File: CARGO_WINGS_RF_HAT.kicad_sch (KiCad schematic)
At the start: 7 parts, among them J1 RPi_GPIO, J2 ESP Prog, J3 Conn_01x04_Socket, J4 Conn_01x04_Socket, J8 S2B-PH-K-S(LF)(SN), U1 DWM1000, U2 ESP32-S3-WROOM-1-N8R2

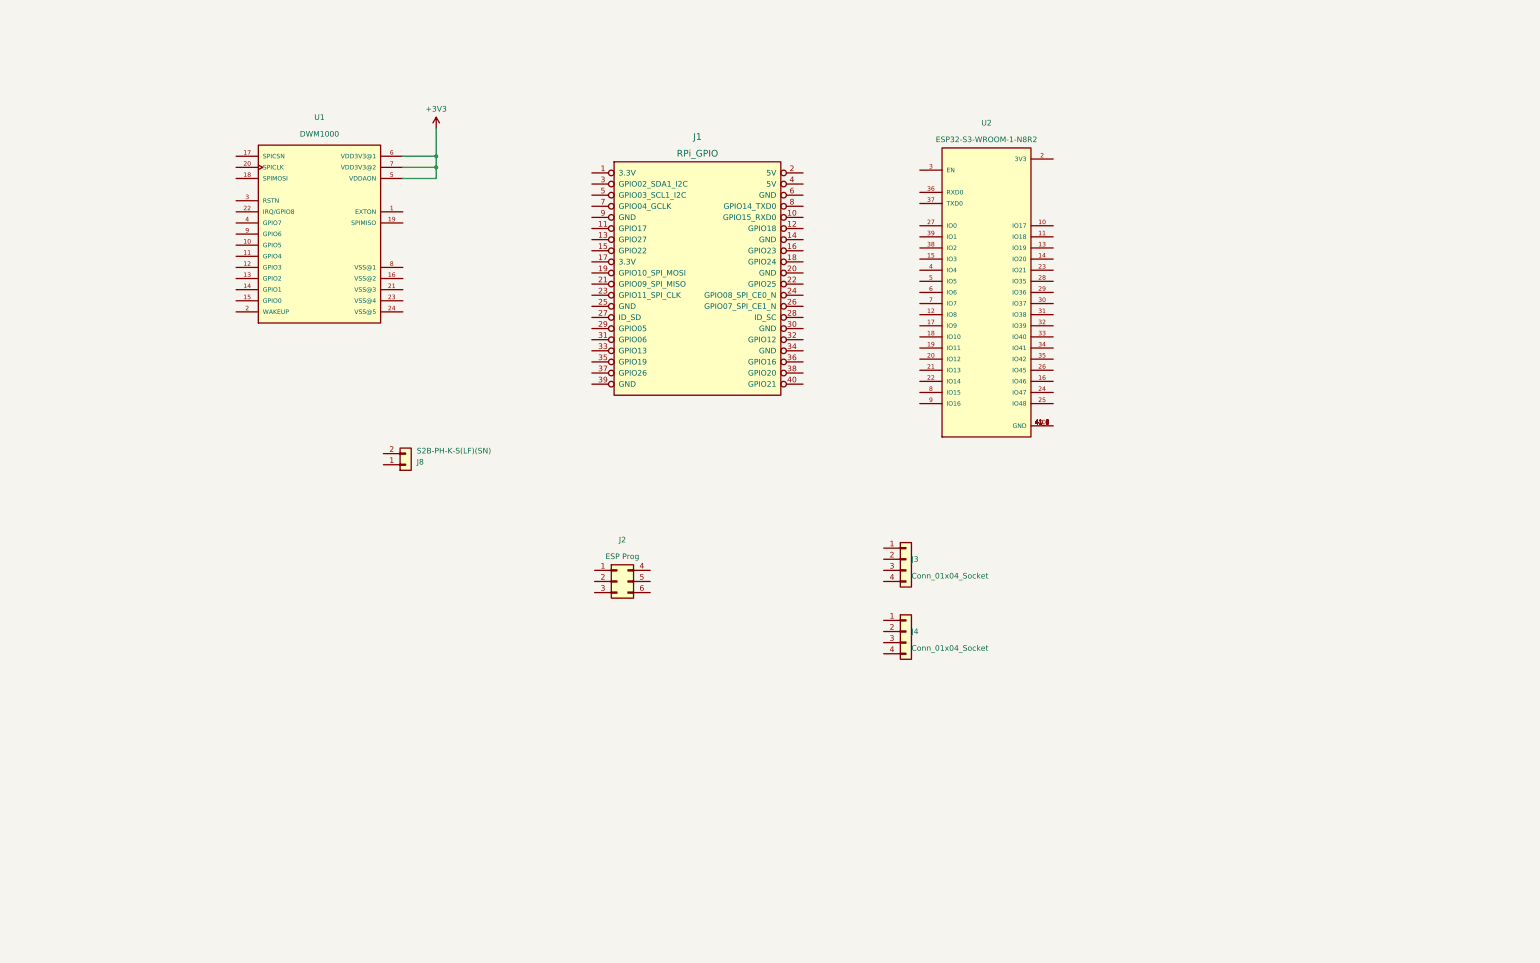
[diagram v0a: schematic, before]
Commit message: Update
- smps added
- booster added 3.7V to 5V
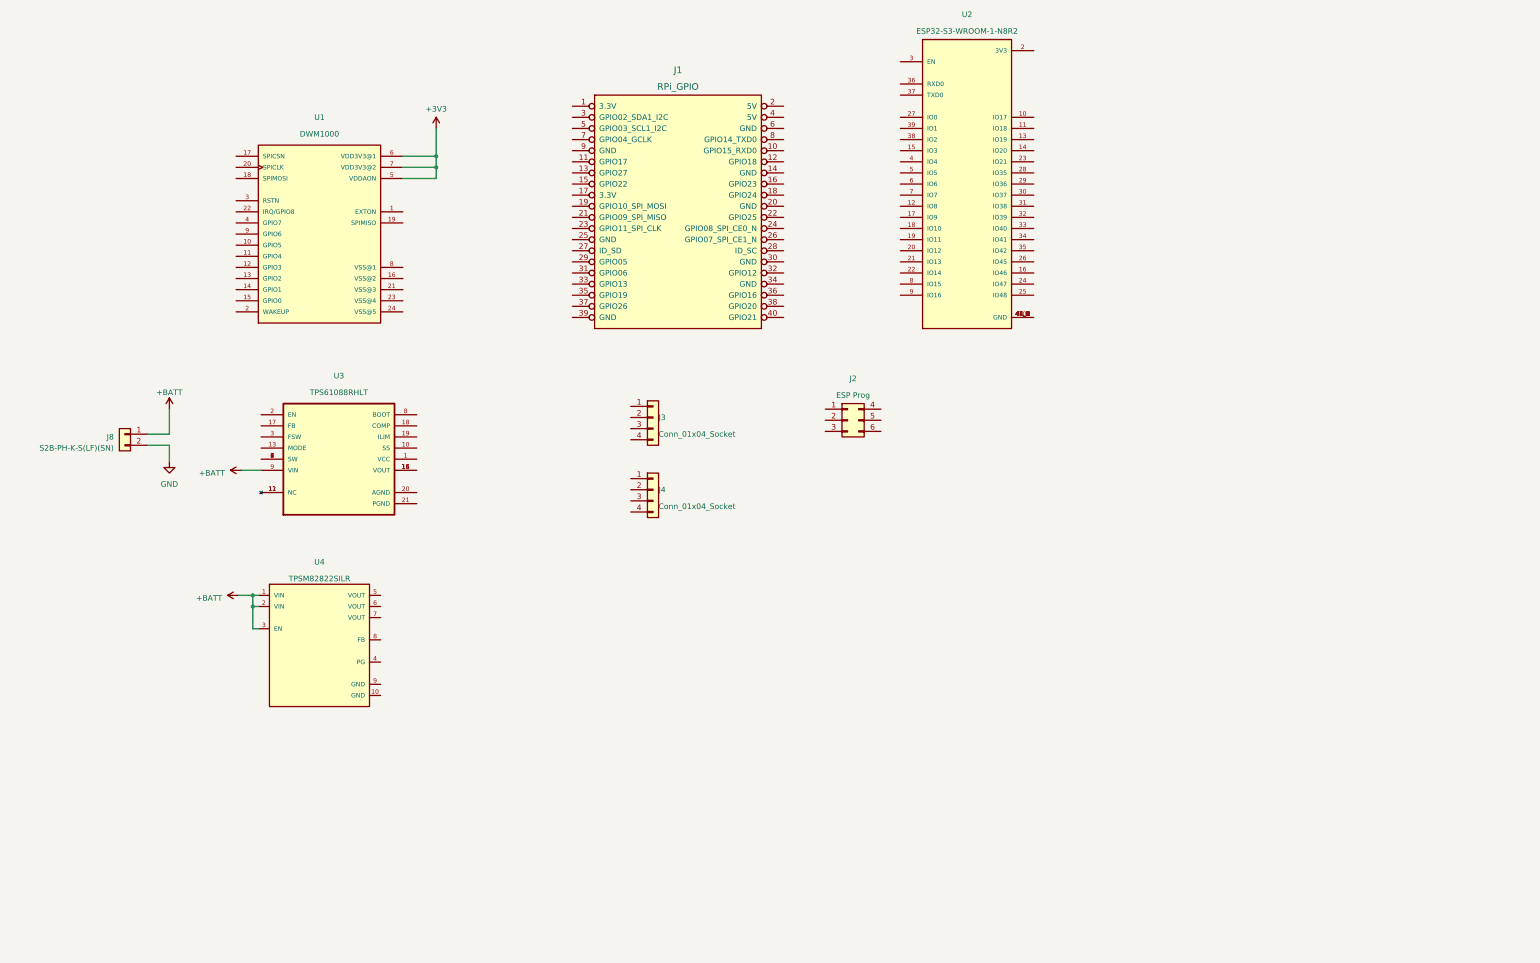
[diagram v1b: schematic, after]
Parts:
- added U3: TPS61088RHLT, IC_MSP430FR2522IRHLR:IC_MSP430FR2522IRHLR, symbol TPS61088RHLT:TPS61088RHLT
- added U4: TPSM82822SILR, Texas_Instruments-SIL0010D-0-0-MFG:Texas_Instruments-SIL0010D-0-0-MFG, symbol Texas_Instruments-SIL0010D-0-0-MFG:TPSM82822SILR
- J2: footprint Connector_PinHeader_1.27mm:PinHeader_2x03_P1.27mm_Vertical -> Connector_PinHeader_1.27mm:PinHeader_2x03_P1.27mm_Vertical_SMD
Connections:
- net +BATT: now reaches J8.1 (Pin_1)
- net +BATT: now also U3.9 (VIN), U4.1 (VIN), U4.2 (VIN), U4.3 (EN)
- net GND: now reaches J8.2 (Pin_2)
- new net: U3.11 (NC), U3.12 (NC)
- new net: U3.14 (VOUT), U3.15 (VOUT), U3.16 (VOUT)
- new net: U3.4 (SW), U3.5 (SW), U3.6 (SW), U3.7 (SW)
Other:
- moved on the sheet: J1, J2, J3, J4, J8, U2

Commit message: update
- power circuit added
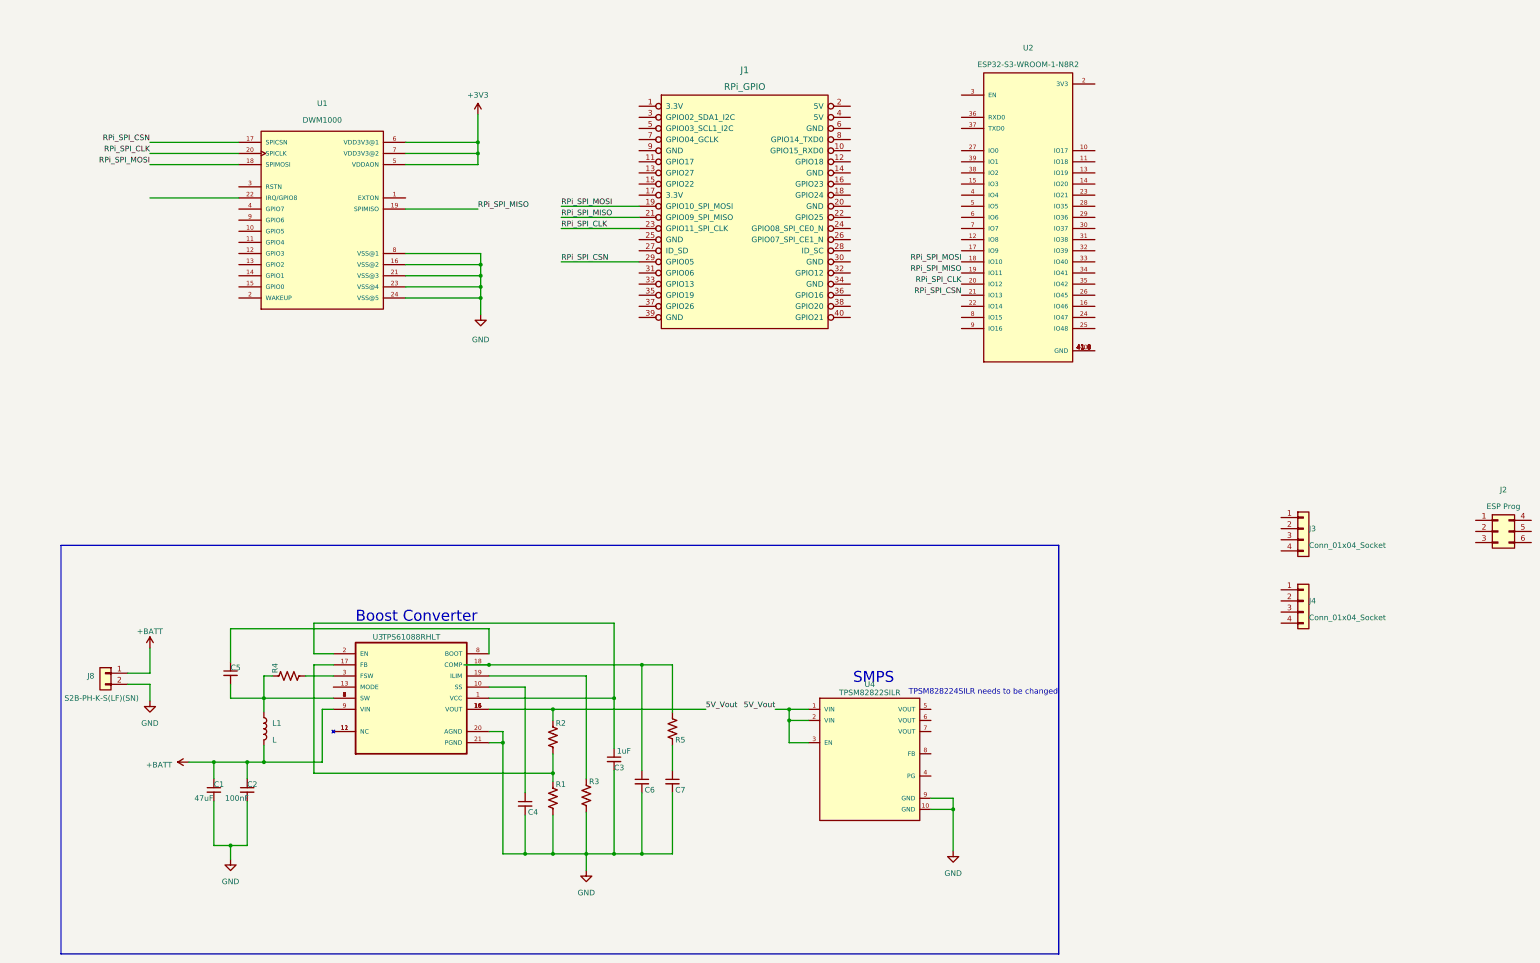
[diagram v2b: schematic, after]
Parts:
- added C1: 47uF, symbol Device:C_Small
- added C2: 100nF, symbol Device:C_Small
- added C3: 1uF, symbol Device:C_Small
- added C4, C5, C6, C7: C_Small, symbol Device:C_Small
- added L1: L, symbol Device:L
- added R1: 69.8kOhm, symbol Device:R_US
- added R2: 220kOhm, symbol Device:R_US
- added R3, R4, R5: R_US, symbol Device:R_US
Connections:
- net +BATT: now also C1.1, C2.1, L1.2; no longer U4.1 (VIN), U4.2 (VIN), U4.3 (EN)
- net GND: now also U1.16 (VSS@2), U1.21 (VSS@3), U1.23 (VSS@4), U1.24 (VSS@5), U1.8 (VSS@1), U3.20 (AGND), U3.21 (PGND), U4.10 (GND), U4.9 (GND), C1.2, C2.2, C3.2, C4.2, C6.2, C7.2, R1.2, R3.2
- net at U3.1 (VCC): now also U3.2 (EN), C3.1
- net at U3.10 (SS): now also C4.1
- net 5V_Vout: now reaches U3.14 (VOUT), U3.15 (VOUT), U3.16 (VOUT)
- net 5V_Vout: now also U4.1 (VIN), U4.2 (VIN), U4.3 (EN), R2.1
- net at U3.17 (FB): now also R1.1, R2.2
- net at U3.18 (COMP): now also C6.1, R5.1
- net at U3.19 (ILIM): now also R3.1
- net at U3.3 (FSW): now also R4.2
- net at U3.4 (SW), U3.5 (SW), U3.6 (SW)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: now also C5.2, L1.1, R4.1
- net at U3.8 (BOOT): now also C5.1
- net RPi_SPI_MOSI: now reaches U2.18 (IO10)
- net RPi_SPI_MOSI: now also J1.19 (GPIO10_SPI_MOSI), U1.18 (SPIMOSI)
- net RPi_SPI_MISO: now reaches U2.19 (IO11)
- net RPi_SPI_MISO: now also J1.21 (GPIO09_SPI_MISO), U1.19 (SPIMISO)
- net RPi_SPI_CLK: now reaches U2.20 (IO12)
- net RPi_SPI_CLK: now also J1.23 (GPIO11_SPI_CLK), U1.20 (SPICLK)
- net RPi_SPI_CSN: now reaches U2.21 (IO13)
- net RPi_SPI_CSN: now also J1.29 (GPIO05), U1.17 (SPICSN)
- new net: C7.1, R5.2
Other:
- note added: "Boost Converter"
- note added: "SMPS"
- note added: "TPSM828224SILR needs to be changed"
- moved on the sheet: J1, J2, J3, J4, J8, U1, U2, U3, U4
